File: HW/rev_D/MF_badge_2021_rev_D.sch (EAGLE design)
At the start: 82 parts, among them IC1 MCP73831, J1 HRO_31_M_12_USB_C, Q1 SI1308EDL-T1-GE3, Q2 DMG3415U-7, Q3 DMG3415U-7, Q4 DMG3415U-7, Q5 Si2305, U1 ESP32-S2-WROOM, U2 AP2112K-3.3, X1 CAPTOUCH_10MM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

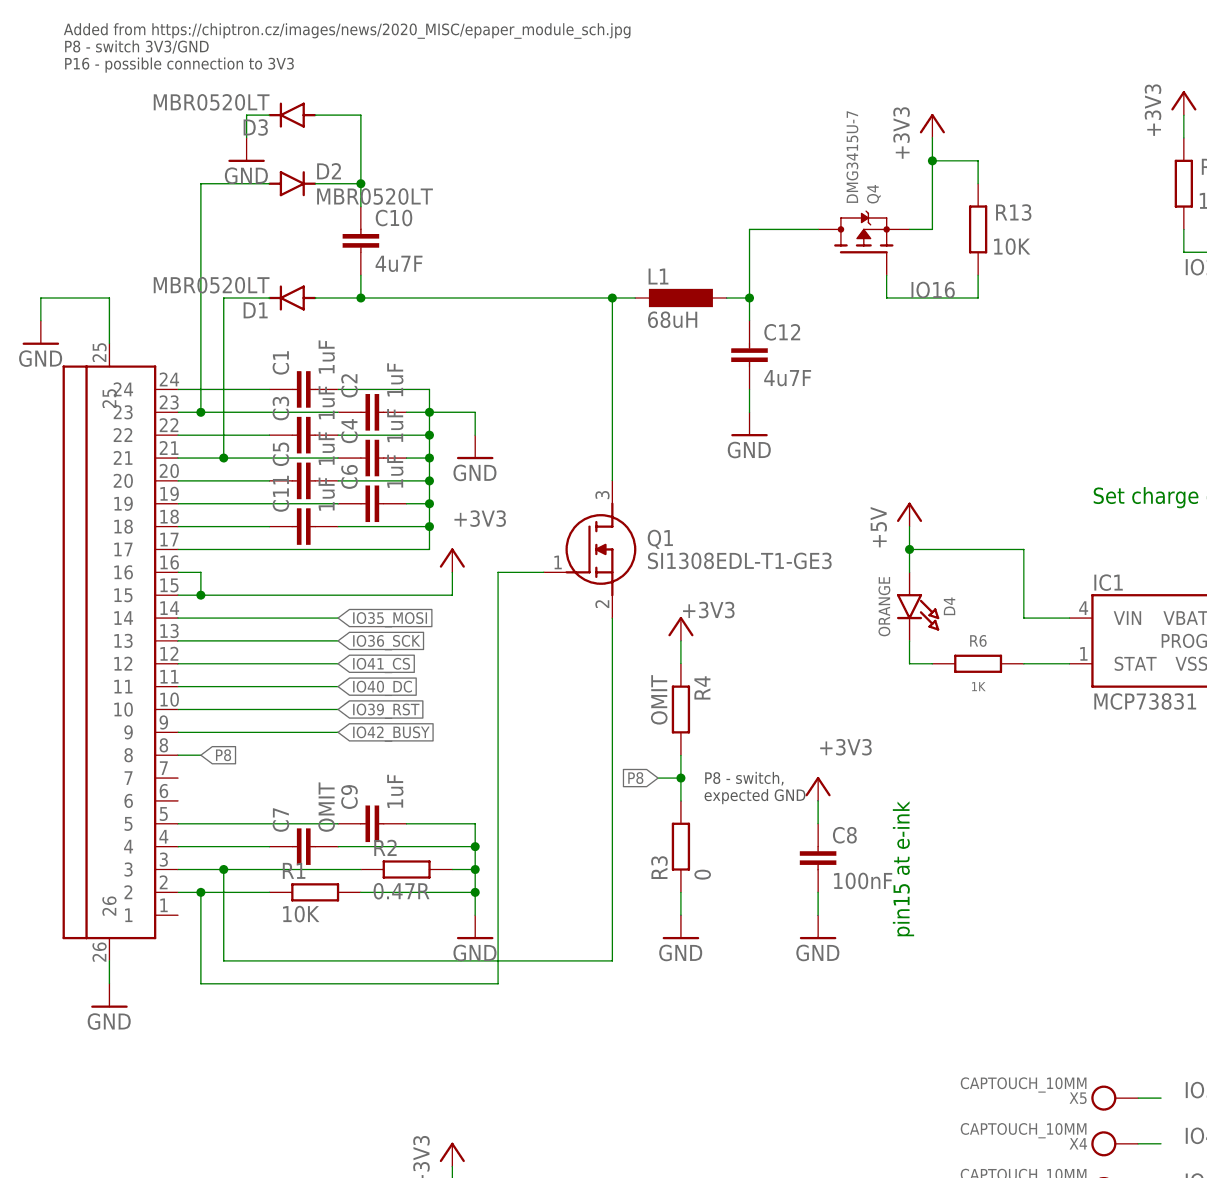
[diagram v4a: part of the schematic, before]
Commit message: Error fix for 3V3 line at e-ink display
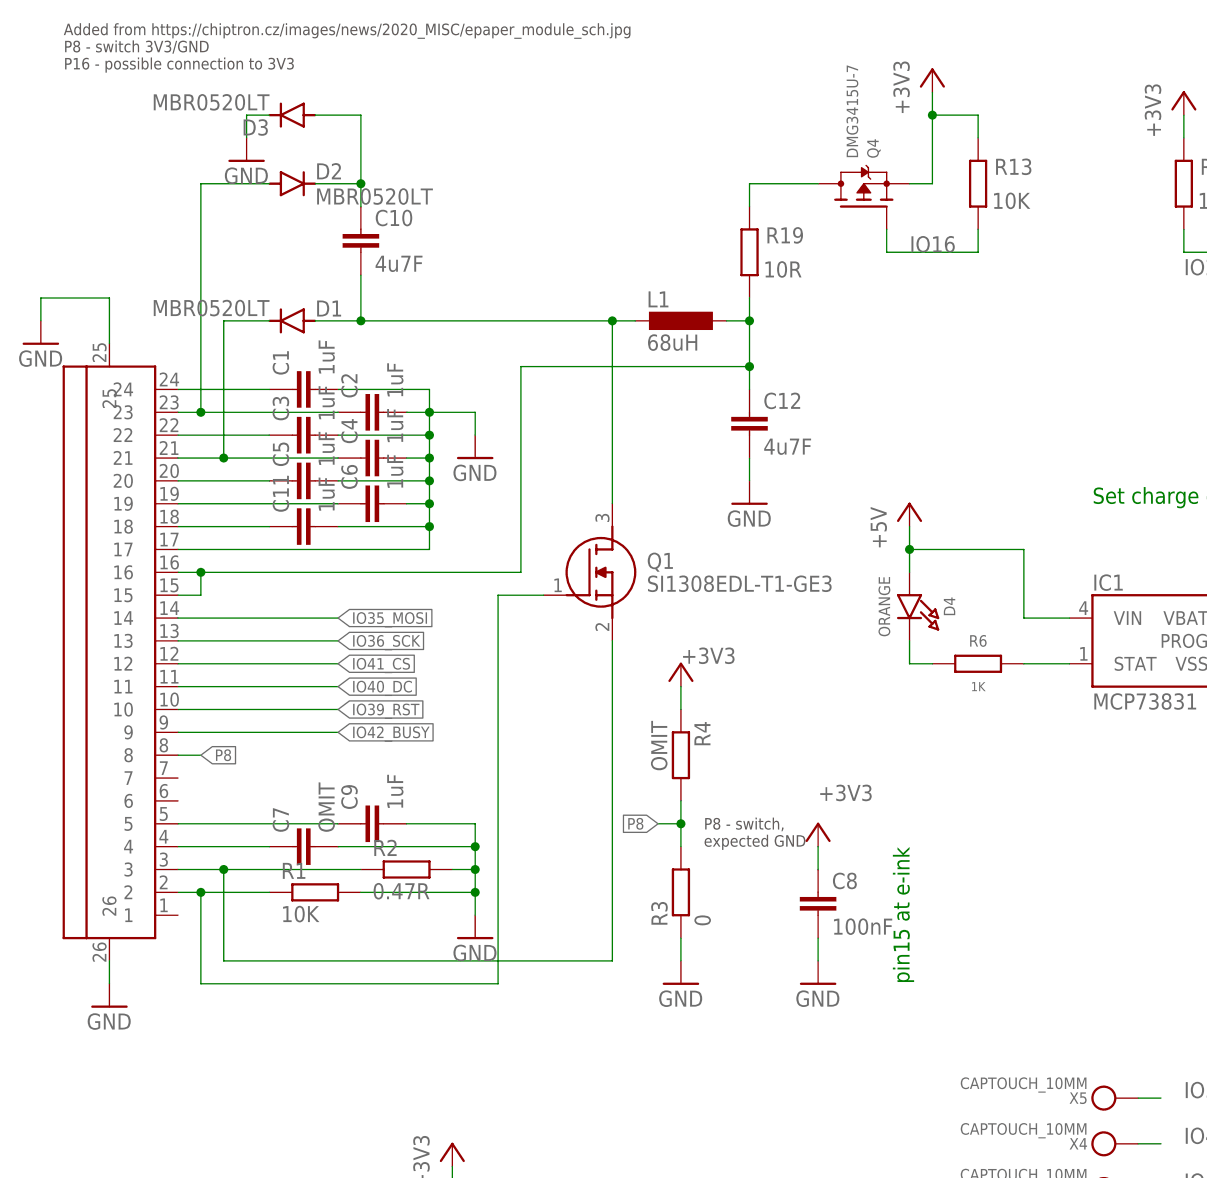
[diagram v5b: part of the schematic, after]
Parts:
- added R19: 10R, rcl:R-EU_R0805
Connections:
- new net N$27: C12.1, L1.1, R19.1, U$1.15, U$1.16
- net +3V3: no longer U$1.15, U$1.16
- net N$26: now also R19.2; no longer C12.1, L1.1
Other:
- moved on the sheet: C12, C8, D1, L1, Q1, Q4, R13, R3, R4

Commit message: Moved 3V3 for e-ink power pins before R19
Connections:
- removed net N$26: Q4.D, R19.2
- new net N$78: C12.1, L1.1, R19.1
- net N$27: now also Q4.D, R19.2; no longer C12.1, L1.1, R19.1
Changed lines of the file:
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@@
 <wire x1="25.4" y1="149.86" x2="25.4" y2="147.32" width="0.1524" layer="91"/>
 <wire x1="25.4" y1="149.86" x2="60.96" y2="149.86" width="0.1524" layer="91"/>
-<wire x1="60.96" y1="149.86" x2="60.96" y2="172.72" width="0.1524" layer="91"/>
+<wire x1="60.96" y1="149.86" x2="60.96" y2="193.04" width="0.1524" layer="91"/>
 <junction x="25.4" y="149.86"/>
-<pinref part="L1" gate="G$1" pin="1"/>
-<pinref part="C12" gate="G$1" pin="1"/>
-<wire x1="83.82" y1="177.8" x2="86.36" y2="177.8" width="0.1524" layer="91"/>
-<wire x1="86.36" y1="177.8" x2="86.36" y2="172.72" width="0.1524" layer="91"/>
-<wire x1="86.36" y1="172.72" x2="86.36" y2="170.18" width="0.1524" layer="91"/>
-<wire x1="60.96" y1="172.72" x2="86.36" y2="172.72" width="0.1524" layer="91"/>
-<junction x="86.36" y="172.72"/>
-<pinref part="R19" gate="G$1" pin="1"/>
-<wire x1="86.36" y1="180.34" x2="86.36" y2="177.8" width="0.1524" layer="91"/>
-<junction x="86.36" y="177.8"/>
-</segment>
-</net>
-<net name="N$26" class="0">
-<segment>
 <pinref part="Q4" gate="G$1" pin="D"/>
 <pinref part="R19" gate="G$1" pin="2"/>
 <wire x1="93.98" y1="193.04" x2="86.36" y2="193.04" width="0.1524" layer="91"/>
 <wire x1="86.36" y1="193.04" x2="86.36" y2="190.5" width="0.1524" layer="91"/>
+<wire x1="60.96" y1="193.04" x2="86.36" y2="193.04" width="0.1524" layer="91"/>
+<junction x="86.36" y="193.04"/>
 </segment>
 </net>
+<net name="N$78" class="1">
+<segment>
+<pinref part="C12" gate="G$1" pin="1"/>
+<pinref part="L1" gate="G$1" pin="1"/>
+<wire x1="83.82" y1="177.8" x2="86.36" y2="177.8" width="0.1524" layer="91"/>
+<pinref part="R19" gate="G$1" pin="1"/>
+<wire x1="86.36" y1="180.34" x2="86.36" y2="177.8" width="0.1524" layer="91"/>
+<junction x="86.36" y="177.8"/>
+<wire x1="86.36" y1="177.8" x2="86.36" y2="170.18" width="0.1524" layer="91"/>
+</segment>
+</net>

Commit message: Update
- added schematics for all versions
- added protoshield files
- added files for rev. D
- README update
- removed unnecessary files
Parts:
- removed FID4: FIDUCIAL_1MM, microbuilder:FIDUCIAL_1MM
- added C23: 10uF, rcl:C-EUC0805
- C14, C20: value 10uF -> 22uF
- C18: value 10uF -> 47uF
- FID1, FID2, FID3: value FIDUCIAL_1MM -> FIDUCIAL""; device microbuilder:FIDUCIAL_1MM -> microbuilder:FIDUCIAL""
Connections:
- net +3V3: now also C23.1
- net GND: now also C23.2
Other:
- moved on the sheet: C14, C20, D5, PWR, Q2, R10, U2
